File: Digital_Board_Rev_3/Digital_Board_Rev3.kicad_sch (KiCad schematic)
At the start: 34 parts, among them J1 Conn_01x02_Male, J11 Conn_01x10_Female, J13 Conn_01x06_Female, J14 Conn_01x06_Female, J15 Conn_01x03_Male, J2 Conn_01x02_Male, J3 Conn_01x06_Male, J4 Conn_01x08_Female, U1 STM32F303R6Tx, Y1 8MHz

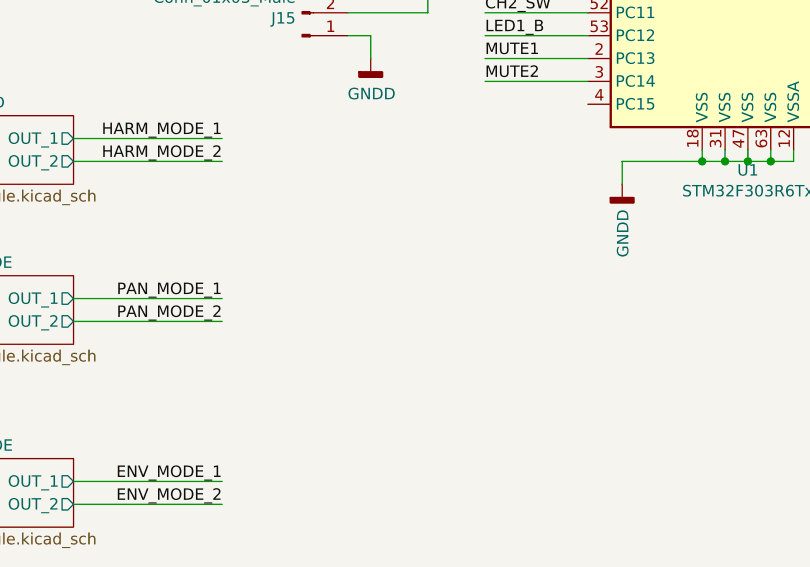
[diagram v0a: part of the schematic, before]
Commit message: Removed unnecessary files, added old gerber outputs
Updated repo to remove files now ignored by updated .gitignore file.
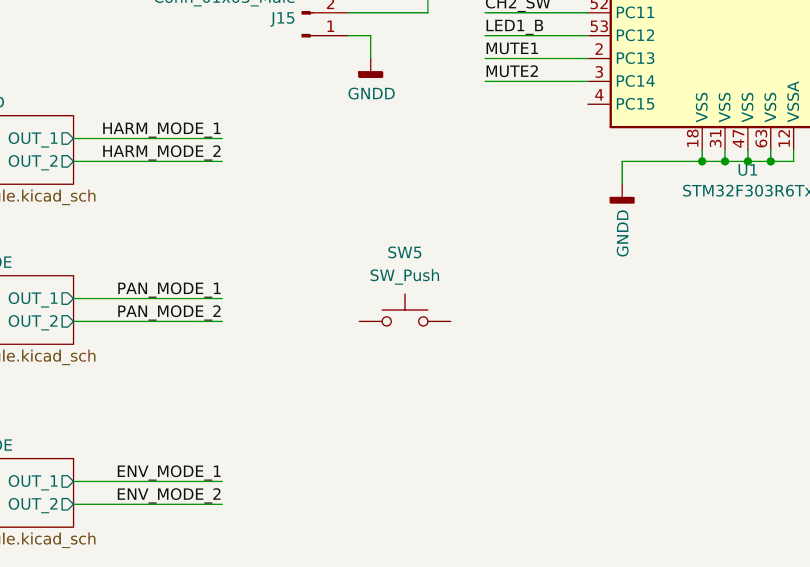
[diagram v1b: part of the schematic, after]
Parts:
- added SW5: SW_Push, symbol Switch:SW_Push
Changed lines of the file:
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@@
+	)
+	(symbol
+		(lib_id "Switch:SW_Push")
+		(at 154.94 226.06 0)
+		(unit 1)
+		(exclude_from_sim no)
+		(in_bom yes)
+		(on_board yes)
+		(dnp no)
+		(fields_autoplaced yes)
+		(property "Reference" "SW5"
+			(at 154.94 218.44 0)
+			(effects
+				(font
+					(size 1.27 1.27)
+				)
+			)
+		)
+		(property "Value" "SW_Push"
+			(at 154.94 220.98 0)
+			(effects
+				(font
+					(size 1.27 1.27)
+				)
+			)
+		)
+		(property "Footprint" ""
+			(at 154.94 220.98 0)
+			(effects
+				(font
+					(size 1.27 1.27)
+				)
+				(hide yes)
+			)
+		)
+		(property "Datasheet" "~"
+			(at 154.94 220.98 0)
+			(effects
+				(font
+					(size 1.27 1.27)
+				)
+				(hide yes)
+			)
+		)
+		(property "Description" "Push button switch, generic, two pins"
+			(at 154.94 226.06 0)
+			(effects
+				(font
+					(size 1.27 1.27)
+				)
+				(hide yes)
+			)
+		)
+		(pin "2"
+		)
+		(pin "1"
+		)
+		(instances
+			(project ""
+				(path "/961bce4d-0f15-4753-8332-e4f92c717c57"
+					(reference "SW5")
+					(unit 1)
+				)
+			)
+		)
 	)
 	(symbol
